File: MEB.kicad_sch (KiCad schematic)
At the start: 6 parts

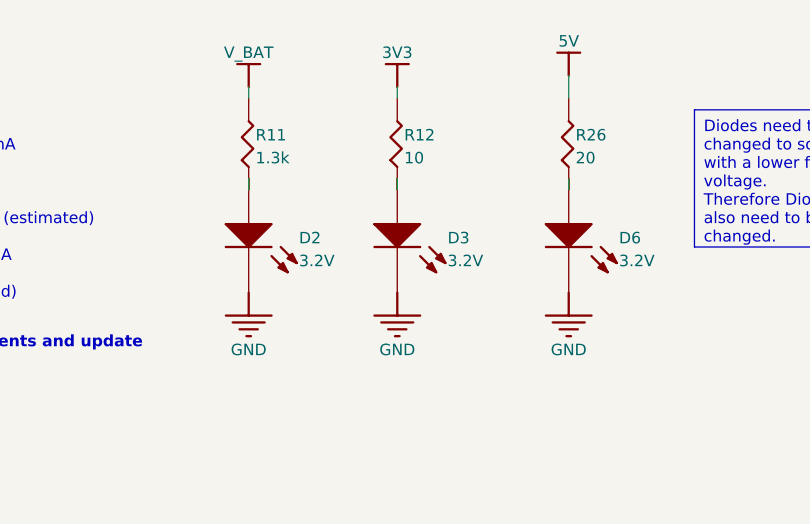
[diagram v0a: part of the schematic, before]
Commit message: updated power and ground symbols in schematic to kicad library version
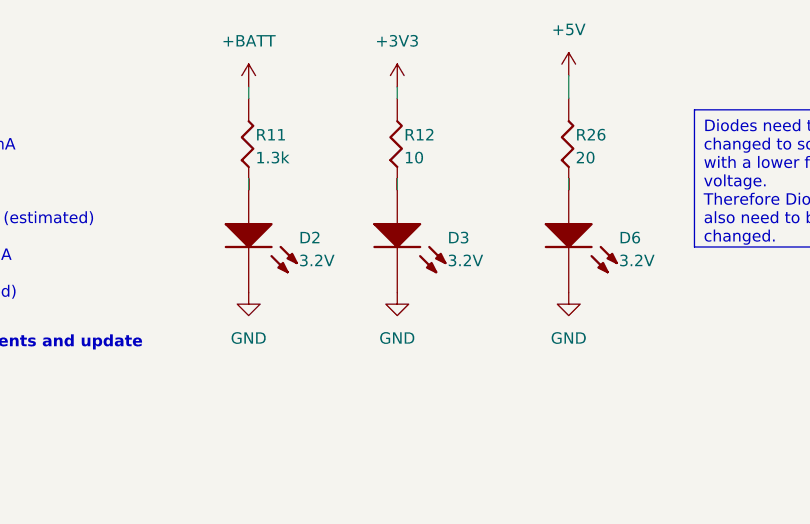
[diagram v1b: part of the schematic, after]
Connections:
- net 3V3 renamed +3V3
- net 5V renamed +5V
- net V_BAT renamed +BATT

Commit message: Fix a variety of small issues
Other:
- sheet Input Headers renamed input_headers
- sheet Output Headers renamed output_headers
- note removed: "Current Consumption"
- note removed: "Verify with measurements and update"
- moved on the sheet: D2, D3, D6, R11, R12, R26
